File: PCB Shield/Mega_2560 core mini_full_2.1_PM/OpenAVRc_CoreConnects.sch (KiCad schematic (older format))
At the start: 19 parts, among them P1 2560-core, P10 RX1TX1, P16 LCD, P6 Micro_sd, P9 SPI, Q1 BSS84

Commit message: Update schematic & pcb
-modify P19 pinout
-connect Q1 to B7 pin's core
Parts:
- Q1: value BSS84 -> IRLML5302
- RV1, RV6: footprint Potentiometers:Potentiometer_Trimmer_Bourns_3296W -> trimpot_5x5_vertical
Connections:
- net BT_OnOff: now also P1.B7 (P28)
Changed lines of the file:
@@
 Sheet 3 7
 Title "Shield Mega2560 core Full"
-Date "2018-02-03"
+Date "2018-02-14"
 Rev "2.10"
 Comp "© Team OpenAVRc"
@@
 $EndComp
 $Comp
-L GND-RESCUE-Mega_2560_core_mini_full_2.0 #PWR51
+L GND-RESCUE-Mega_2560_core_mini_full_2.0 #PWR045
 U 1 1 59C5DDBC
 P 4250 4450
-F 0 "#PWR51" H 4250 4200 50  0001 C CNN
+F 0 "#PWR045" H 4250 4200 50  0001 C CNN
 F 1 "GND" H 4250 4300 50  0000 C CNN
 F 2 "" H 4250 4450 50  0000 C CNN
@@
 $EndComp
 $Comp
-L VCC #PWR49
+L VCC #PWR046
 U 1 1 59C5DDC2
 P 3900 4700
-F 0 "#PWR49" H 3900 4550 50  0001 C CNN
+F 0 "#PWR046" H 3900 4550 50  0001 C CNN
 F 1 "VCC" V 3900 4900 50  0000 C CNN
 F 2 "" H 3900 4700 50  0000 C CNN
@@
 $EndComp
 $Comp
-L GND-RESCUE-Mega_2560_core_mini_full_2.0 #PWR47
+L GND-RESCUE-Mega_2560_core_mini_full_2.0 #PWR047
 U 1 1 59C5DDC8
 P 3400 1700
-F 0 "#PWR47" H 3400 1450 50  0001 C CNN
+F 0 "#PWR047" H 3400 1450 50  0001 C CNN
 F 1 "GND" H 3400 1550 50  0000 C CNN
 F 2 "" H 3400 1700 50  0000 C CNN
@@
 $EndComp
 $Comp
-L VCC #PWR48
+L VCC #PWR048
 U 1 1 59C5DDCE
 P 3700 1700
-F 0 "#PWR48" H 3700 1550 50  0001 C CNN
+F 0 "#PWR048" H 3700 1550 50  0001 C CNN
 F 1 "VCC" H 3700 1850 50  0000 C CNN
 F 2 "" H 3700 1700 50  0000 C CNN
@@
 Mosi
 $Comp
-L GND-RESCUE-Mega_2560_core_mini_full_2.0 #PWR55
+L GND-RESCUE-Mega_2560_core_mini_full_2.0 #PWR049
 U 1 1 59C5DDDC
 P 4900 2450
-F 0 "#PWR55" H 4900 2200 50  0001 C CNN
+F 0 "#PWR049" H 4900 2200 50  0001 C CNN
 F 1 "GND" V 4900 2250 50  0000 C CNN
 F 2 "" H 4900 2450 50  0000 C CNN
@@
 $EndComp
 $Comp
-L VCC #PWR54
+L VCC #PWR050
 U 1 1 59C5DDE2
 P 4900 2250
-F 0 "#PWR54" H 4900 2100 50  0001 C CNN
+F 0 "#PWR050" H 4900 2100 50  0001 C CNN
 F 1 "VCC" V 4900 2450 50  0000 C CNN
 F 2 "" H 4900 2250 50  0000 C CNN
@@
 $EndComp
 $Comp
-L VCC #PWR46
+L VCC #PWR051
 U 1 1 59C5DDE8
 P 2600 2100
-F 0 "#PWR46" H 2600 1950 50  0001 C CNN
+F 0 "#PWR051" H 2600 1950 50  0001 C CNN
 F 1 "VCC" V 2600 2300 50  0000 C CNN
 F 2 "" H 2600 2100 50  0000 C CNN
@@
 Lcd_bla
 $Comp
-L GND-RESCUE-Mega_2560_core_mini_full_2.0 #PWR44
+L GND-RESCUE-Mega_2560_core_mini_full_2.0 #PWR052
 U 1 1 59C5DE25
 P 1850 4450
-F 0 "#PWR44" H 1850 4200 50  0001 C CNN
+F 0 "#PWR052" H 1850 4200 50  0001 C CNN
 F 1 "GND" H 1850 4300 50  0000 C CNN
 F 2 "" H 1850 4450 50  0000 C CNN
@@
 $EndComp
 $Comp
-L GND-RESCUE-Mega_2560_core_mini_full_2.0 #PWR45
+L GND-RESCUE-Mega_2560_core_mini_full_2.0 #PWR053
 U 1 1 59C5DE2D
 P 2350 5300
-F 0 "#PWR45" H 2350 5050 50  0001 C CNN
+F 0 "#PWR053" H 2350 5050 50  0001 C CNN
 F 1 "GND" H 2350 5150 50  0000 C CNN
 F 2 "" H 2350 5300 50  0000 C CNN
@@
 $EndComp
 $Comp
-L GND-RESCUE-Mega_2560_core_mini_full_2.0 #PWR52
+L GND-RESCUE-Mega_2560_core_mini_full_2.0 #PWR054
 U 1 1 59C5DE45
 P 4550 4450
-F 0 "#PWR52" H 4550 4200 50  0001 C CNN
+F 0 "#PWR054" H 4550 4200 50  0001 C CNN
 F 1 "GND" H 4550 4300 50  0000 C CNN
 F 2 "" H 4550 4450 50  0000 C CNN
@@
 $EndComp
 $Comp
-L GND-RESCUE-Mega_2560_core_mini_full_2.0 #PWR50
+L GND-RESCUE-Mega_2560_core_mini_full_2.0 #PWR055
 U 1 1 59C5DE66
 P 4150 4950
-F 0 "#PWR50" H 4150 4700 50  0001 C CNN
+F 0 "#PWR055" H 4150 4700 50  0001 C CNN
 F 1 "GND" H 4150 4800 50  0000 C CNN
 F 2 "" H 4150 4950 50  0000 C CNN
@@
 $EndComp
 $Comp
-L GND-RESCUE-Mega_2560_core_mini_full_2.0 #PWR43
+L GND-RESCUE-Mega_2560_core_mini_full_2.0 #PWR056
 U 1 1 59C5DE7A
 P 1400 2100
-F 0 "#PWR43" H 1400 1850 50  0001 C CNN
+F 0 "#PWR056" H 1400 1850 50  0001 C CNN
 F 1 "GND" H 1400 1950 50  0000 C CNN
 F 2 "" H 1400 2100 50  0000 C CNN
@@
 $EndComp
 $Comp
-L GND-RESCUE-Mega_2560_core_mini_full_2.0 #PWR53
+L GND-RESCUE-Mega_2560_core_mini_full_2.0 #PWR057
 U 1 1 59C5DE80
 P 4850 2100
-F 0 "#PWR53" H 4850 1850 50  0001 C CNN
+F 0 "#PWR057" H 4850 1850 50  0001 C CNN
 F 1 "GND" V 4850 1900 50  0000 C CNN
 F 2 "" H 4850 2100 50  0000 C CNN
@@
 $EndComp
 $Comp
-L GND-RESCUE-Mega_2560_core_mini_full_2.0 #PWR57
+L GND-RESCUE-Mega_2560_core_mini_full_2.0 #PWR058
 U 1 1 59C5BE4B
 P 7050 2100
-F 0 "#PWR57" H 7050 1850 50  0001 C CNN
+F 0 "#PWR058" H 7050 1850 50  0001 C CNN
 F 1 "GND" H 7050 1950 50  0000 C CNN
 F 2 "" H 7050 2100 50  0000 C CNN
@@
 $EndComp
 $Comp
-L VCC #PWR56
+L VCC #PWR059
 U 1 1 59C5BE51
 P 6750 2100
-F 0 "#PWR56" H 6750 1950 50  0001 C CNN
+F 0 "#PWR059" H 6750 1950 50  0001 C CNN
 F 1 "VCC" H 6750 2250 50  0000 C CNN
 F 2 "" H 6750 2100 50  0000 C CNN
@@
 Miso
 $Comp
-L GND-RESCUE-Mega_2560_core_mini_full_2.0 #PWR61
+L GND-RESCUE-Mega_2560_core_mini_full_2.0 #PWR060
 U 1 1 59C5BE5B
 P 8750 1800
-F 0 "#PWR61" H 8750 1550 50  0001 C CNN
+F 0 "#PWR060" H 8750 1550 50  0001 C CNN
 F 1 "GND" H 8750 1650 50  0000 C CNN
 F 2 "" H 8750 1800 50  0000 C CNN
@@
 Lcd_cs
 $Comp
-L GND-RESCUE-Mega_2560_core_mini_full_2.0 #PWR64
+L GND-RESCUE-Mega_2560_core_mini_full_2.0 #PWR061
 U 1 1 59C5BE7F
 P 10550 2050
-F 0 "#PWR64" H 10550 1800 50  0001 C CNN
+F 0 "#PWR061" H 10550 1800 50  0001 C CNN
 F 1 "GND" H 10550 1900 50  0000 C CNN
 F 2 "" H 10550 2050 50  0000 C CNN
@@
 Lcd_db5
 $Comp
-L GND-RESCUE-Mega_2560_core_mini_full_2.0 #PWR62
+L GND-RESCUE-Mega_2560_core_mini_full_2.0 #PWR062
 U 1 1 59C5BE86
 P 9150 2650
-F 0 "#PWR62" H 9150 2400 50  0001 C CNN
+F 0 "#PWR062" H 9150 2400 50  0001 C CNN
 F 1 "GND" H 9150 2500 50  0000 C CNN
 F 2 "" H 9150 2650 50  0000 C CNN
@@
 F 0 "RV6" V 10100 2700 50  0000 C CNN
 F 1 "500" V 10200 2700 50  0000 C CNN
-F 2 "Potentiometers:Potentiometer_Trimmer_Bourns_3296W" H 10200 2700 50  0001 C CNN
+F 2 "trimpot_5x5_vertical" H 10200 2700 50  0001 C CNN
 F 3 "" H 10200 2700 50  0000 C CNN
 	1    10200 2700
@@
 F 0 "RV1" V 9050 2400 50  0000 C CNN
 F 1 "10K" V 9150 2400 50  0000 C CNN
-F 2 "Potentiometers:Potentiometer_Trimmer_Bourns_3296W" H 9150 2400 50  0001 C CNN
+F 2 "trimpot_5x5_vertical" H 9150 2400 50  0001 C CNN
 F 3 "" H 9150 2400 50  0000 C CNN
 	1    9150 2400
@@
 $EndComp
 $Comp
-L GND-RESCUE-Mega_2560_core_mini_full_2.0 #PWR59
+L GND-RESCUE-Mega_2560_core_mini_full_2.0 #PWR063
 U 1 1 59C5BEA8
 P 8100 4850
-F 0 "#PWR59" H 8100 4600 50  0001 C CNN
+F 0 "#PWR063" H 8100 4600 50  0001 C CNN
 F 1 "GND" H 8100 4700 50  0000 C CNN
 F 2 "" H 8100 4850 50  0000 C CNN
@@
 $EndComp
 $Comp
-L GND-RESCUE-Mega_2560_core_mini_full_2.0 #PWR60
+L GND-RESCUE-Mega_2560_core_mini_full_2.0 #PWR064
 U 1 1 59C5BEAE
 P 8500 5200
-F 0 "#PWR60" H 8500 4950 50  0001 C CNN
+F 0 "#PWR064" H 8500 4950 50  0001 C CNN
 F 1 "GND" H 8500 5050 50  0000 C CNN
 F 2 "" H 8500 5200 50  0000 C CNN
@@
 P 9100 4800
 F 0 "Q1" V 9000 5000 60  0000 R CNN
-F 1 "BSS84" V 9300 4950 60  0000 R CNN
+F 1 "IRLML5302" V 9300 5050 60  0000 R CNN
 F 2 "" H 9100 4800 60  0000 C CNN
 F 3 "" H 9100 4800 60  0000 C CNN
@@
 $EndComp
 $Comp
-L VCC #PWR63
+L VCC #PWR065
 U 1 1 59E0DFF9
 P 9600 4550
-F 0 "#PWR63" H 9600 4400 50  0001 C CNN
+F 0 "#PWR065" H 9600 4400 50  0001 C CNN
 F 1 "VCC" H 9600 4700 50  0000 C CNN
 F 2 "" H 9600 4550 50  0000 C CNN
@@
 	9500 5300 10000 5300
 Connection ~ 9100 5100
-Text Label 10000 5300 2    60   ~ 0
-BT_OnOff
 $Comp
 L R-RESCUE-Mega_2560_core_mini_full_2.0 R40
@@
 	7500 5050 7400 5050
 $Comp
-L GND-RESCUE-Mega_2560_core_mini_full_2.0 #PWR58
+L GND-RESCUE-Mega_2560_core_mini_full_2.0 #PWR066
 U 1 1 59EF4C7A
 P 7400 5050
-F 0 "#PWR58" H 7400 4800 50  0001 C CNN
+F 0 "#PWR066" H 7400 4800 50  0001 C CNN
 F 1 "GND" H 7400 4900 50  0000 C CNN
 F 2 "" H 7400 5050 50  0000 C CNN
@@
 	1    0    0    -1
 $EndComp
+Wire Wire Line
+	1850 3550 1450 3550
+Text GLabel 1450 3550 0    60   Output ~ 0
+BT_OnOff
+Text GLabel 10000 5300 2    60   Input ~ 0
+BT_OnOff
 $EndSCHEMATC

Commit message: Update schemtaic & PCB files
-update P19 pinout .
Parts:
- Q1: value IRLML5302 -> IRLML5203
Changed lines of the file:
@@
 Sheet 3 7
 Title "Shield Mega2560 core Full"
-Date "2018-02-14"
+Date "2018-02-15"
 Rev "2.10"
 Comp "© Team OpenAVRc"
@@
 P 9100 4800
 F 0 "Q1" V 9000 5000 60  0000 R CNN
-F 1 "IRLML5302" V 9300 5050 60  0000 R CNN
+F 1 "IRLML5203" V 9300 5050 60  0000 R CNN
 F 2 "" H 9100 4800 60  0000 C CNN
 F 3 "" H 9100 4800 60  0000 C CNN

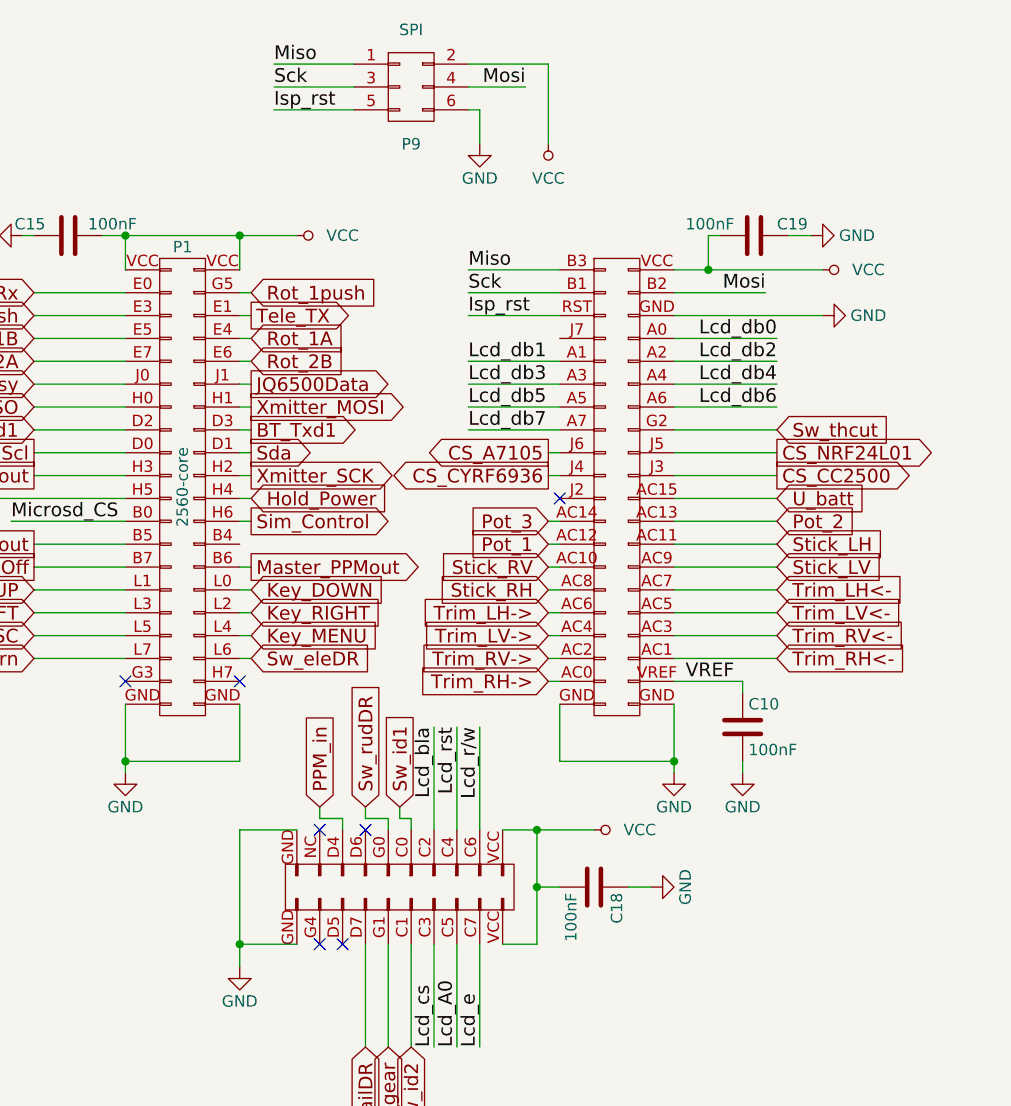
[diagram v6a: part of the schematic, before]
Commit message: Update schematic é pcb files
-replace u2 and u3 by 2 74lvc1g3157gv
-remove p15 and p3
-add ftdi connector as p3
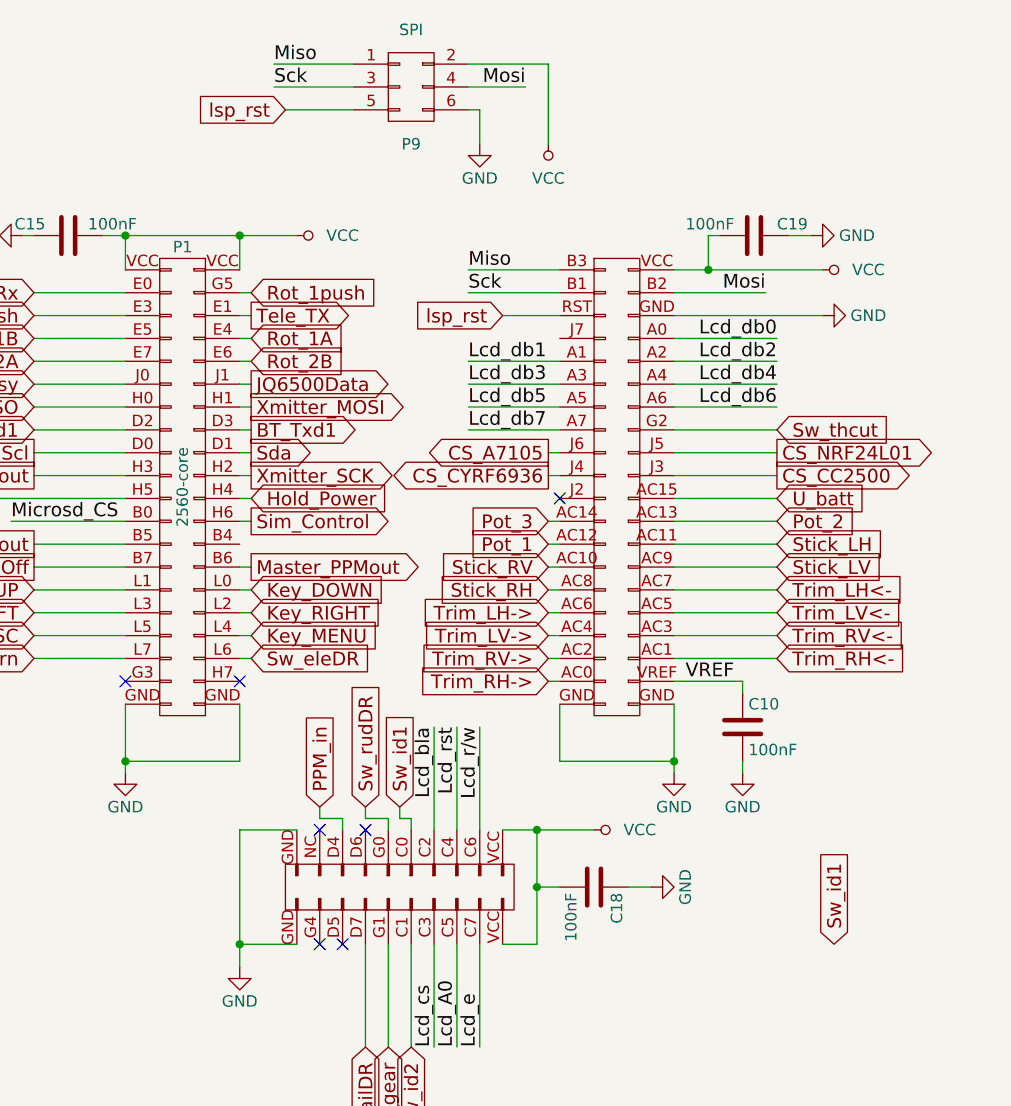
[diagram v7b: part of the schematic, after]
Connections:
- net Isp_rst renamed lsp_rst
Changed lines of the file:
@@
 Sheet 3 7
 Title "Shield Mega2560 core Full"
-Date "2018-02-21"
+Date "2018-02-25"
 Rev "2.10"
 Comp "© Team OpenAVRc"
@@
 	-1   0    0    1
 $EndComp
-Text Label 3350 2450 0    60   ~ 0
-Isp_rst
-Text Label 2500 1550 0    60   ~ 0
-Isp_rst
 Text Label 2500 1450 0    60   ~ 0
 Sck
@@
 Connection ~ 2350 2100
 Wire Wire Line
-	2850 1550 2500 1550
-Wire Wire Line
 	2850 1450 2500 1450
 Wire Wire Line
@@
 Wire Wire Line
 	3750 2350 3350 2350
-Wire Wire Line
-	3750 2450 3350 2450
 Wire Wire Line
 	2500 1350 2850 1350
@@
 Text GLabel 10000 5300 2    60   Input ~ 0
 BT_OnOff
+Text GLabel 4950 5200 1    60   Input ~ 0
+Sw_id1
+Text GLabel 3500 2450 0    60   Input ~ 0
+lsp_rst
+Wire Wire Line
+	3750 2450 3500 2450
+Text GLabel 2550 1550 0    60   Input ~ 0
+lsp_rst
+Wire Wire Line
+	2850 1550 2550 1550
 $EndSCHEMATC

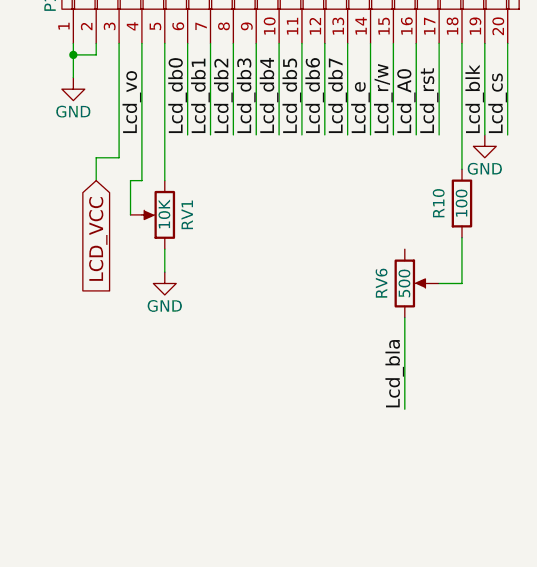
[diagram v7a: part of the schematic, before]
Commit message: Update schematic & pcb files
-add 220ohm on Tele_TX
-update rv1 & rv2 values
-finish pcb .
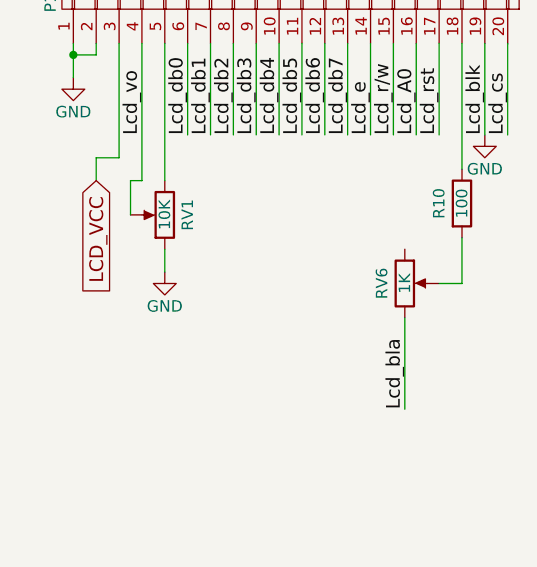
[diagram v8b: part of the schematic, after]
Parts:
- RV6: value 500 -> 1K
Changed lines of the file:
@@
 Sheet 3 7
 Title "Shield Mega2560 core Full"
-Date "2018-02-25"
+Date "2018-02-28"
 Rev "2.10"
 Comp "© Team OpenAVRc"
@@
 P 10200 2700
 F 0 "RV6" V 10100 2700 50  0000 C CNN
-F 1 "500" V 10200 2700 50  0000 C CNN
+F 1 "1K" V 10200 2700 50  0000 C CNN
 F 2 "trimpot_5x5_vertical" H 10200 2700 50  0001 C CNN
 F 3 "" H 10200 2700 50  0000 C CNN
